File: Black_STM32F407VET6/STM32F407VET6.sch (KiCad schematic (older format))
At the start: 97 parts, among them J1 T0, J10 - HotBed +, J11 Heater0, J12 X-, J13 Y-, J14 Z-, J15 Z+, J16 USB_B, J17 X_logic, J18 Y_logic, J19 Z_logic, J2 T1, J20 E0_logic, J22 Left, J23 EXP2, J24 LCD2004, J25 Bottom, J26 Right, J27 Z_motor, J28 LIGHTS, J29 Z, J3 TB, J30 Z, J33 X_motor, J34 Y_motor, J36 E0_motor, J38 X, J39 Y, J4 TC, J41 E0, J43 Heater1, J44 COM, J47 I2C, J48 SPI, J49 SPI, J5 + VIN -, J50 SDIO, J51 Servo, J52 Servo, J53 PowerSelect, J54 Power, J55 PD11, J56 Power, J6 Fan3, J7 Fan2, J8 Fan1, J9 Fan0, Q1 BCX70, Q10 BCX70, Q11 BCX70, Q12 IRLR8726PBF, Q13 IRLR8726PBF, Q14 IRLR8726PBF, Q2 BCX70, Q3 BCX70, Q4 IRLML0030TRPBF, Q5 BCX70, Q6 IRLML0030TRPBF, Q7 IRLML0030TRPBF, Q8 IRLML0030TRPBF, Q9 BCX70, SW1 Boot0, U5 AT24CS01-SSHM

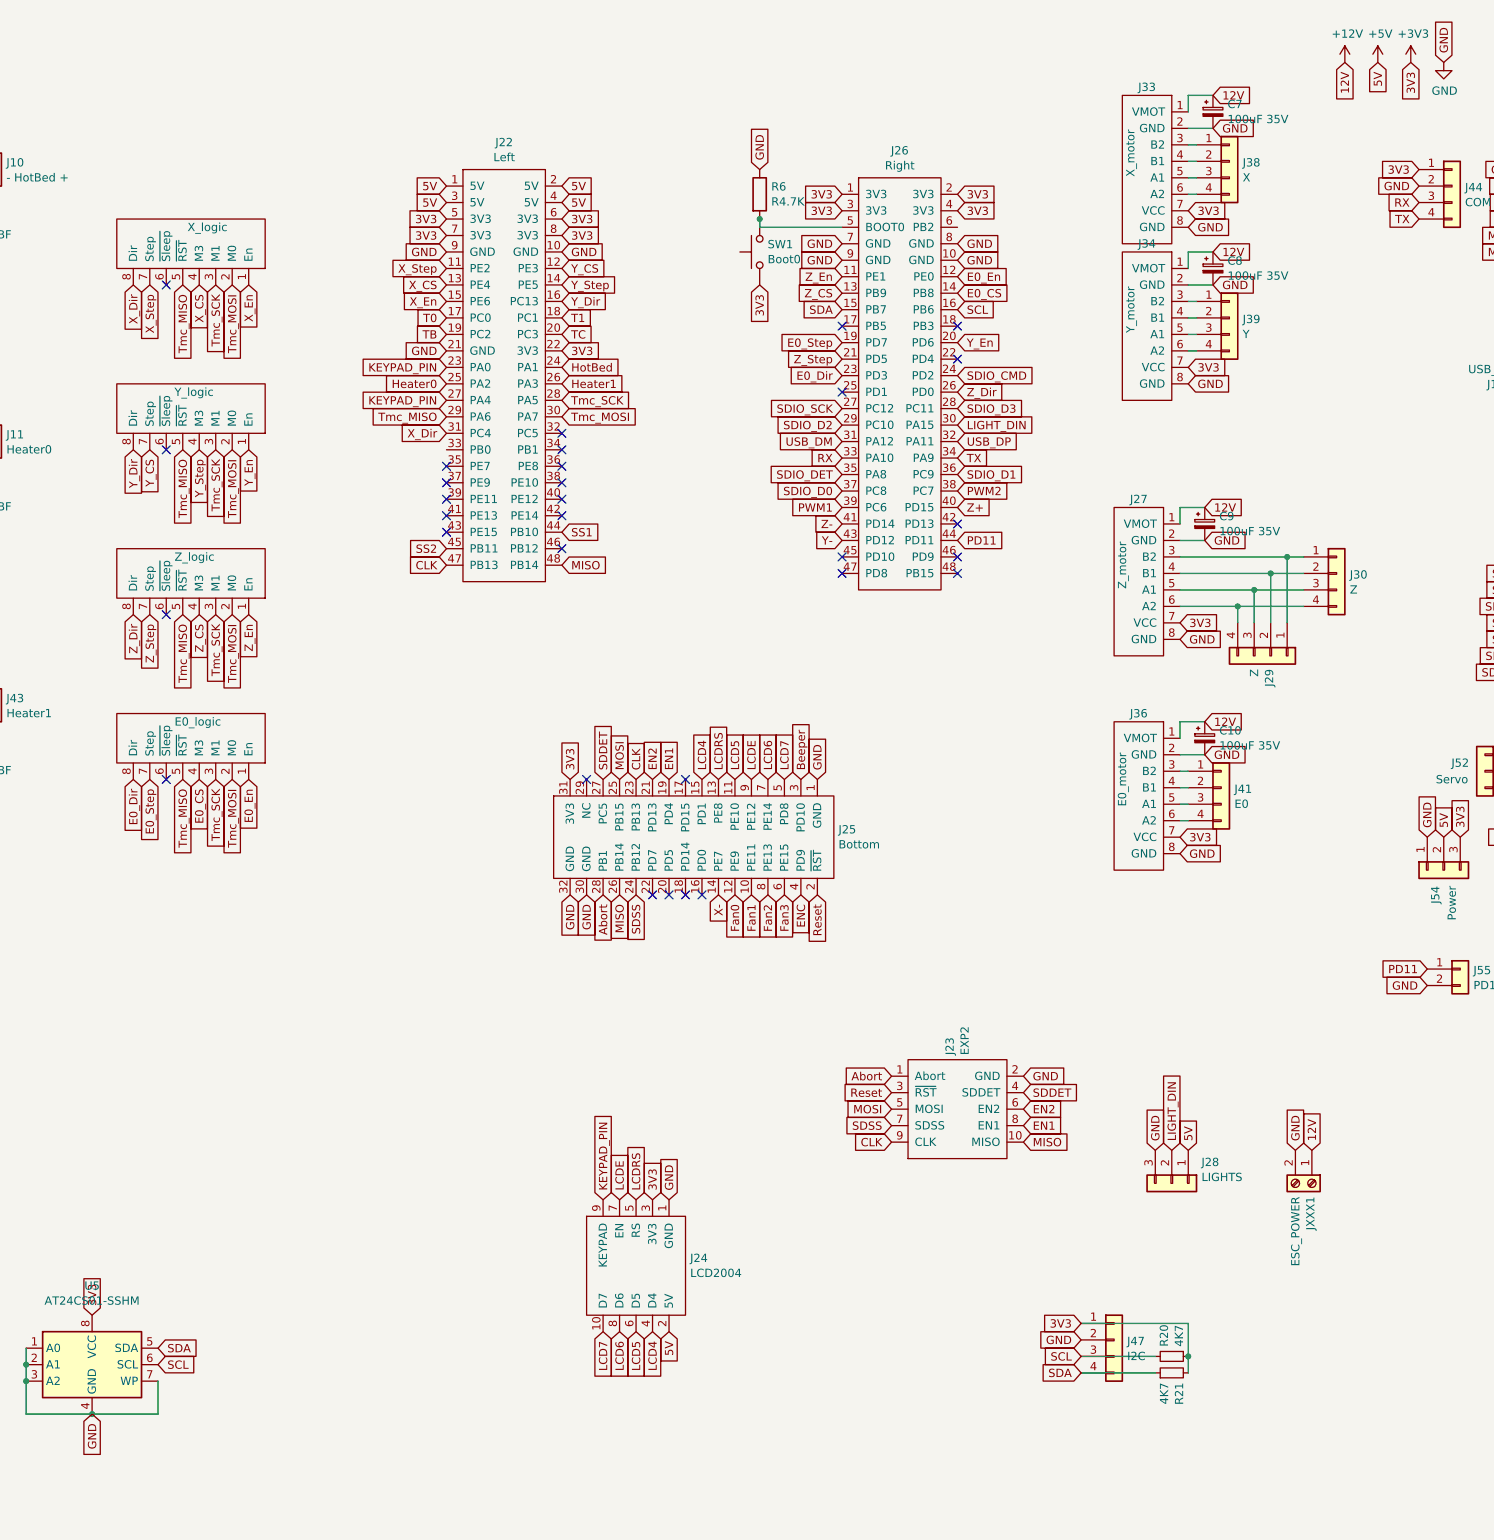
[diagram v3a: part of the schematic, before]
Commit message: Rework of the PCB, made footprint for the motor drivers.
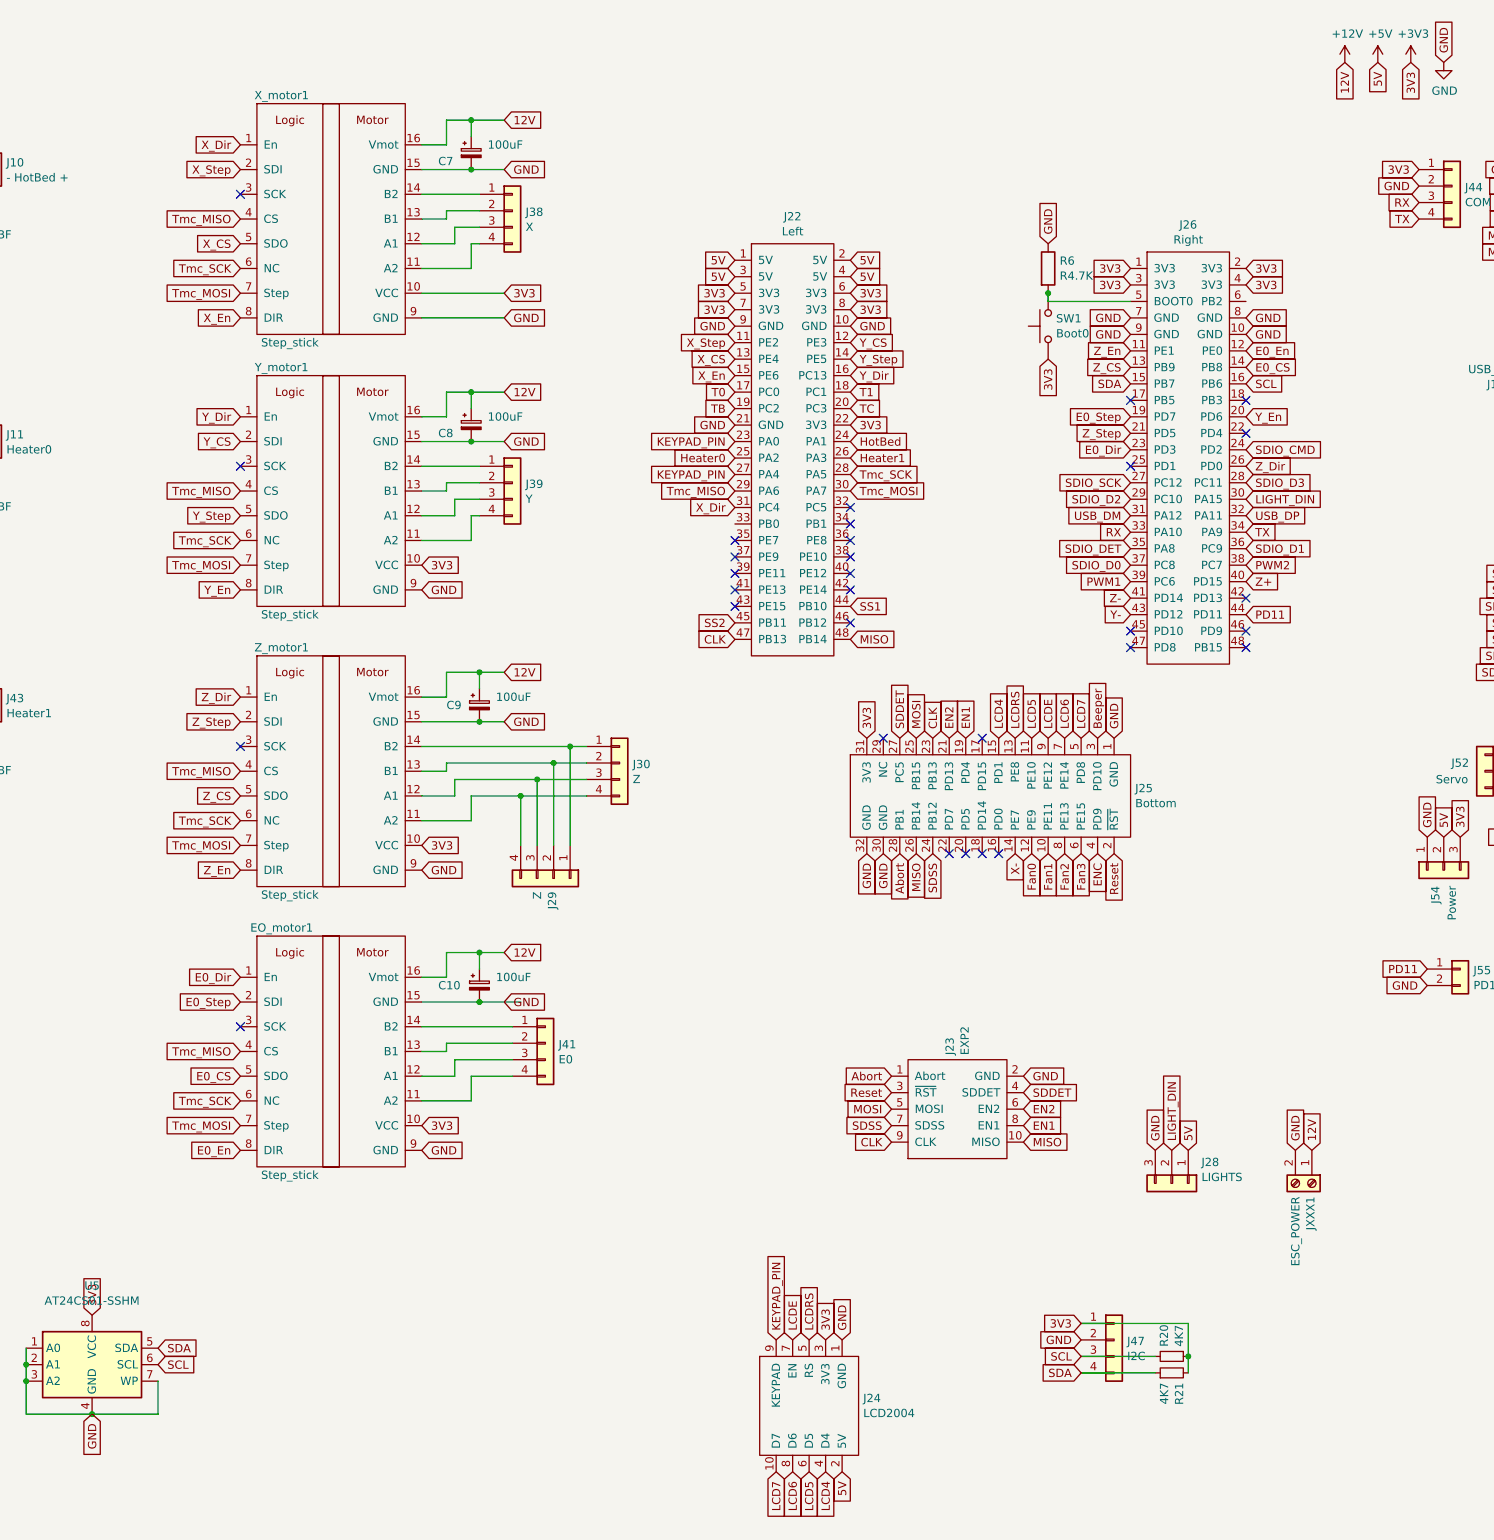
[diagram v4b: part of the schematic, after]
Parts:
- removed J17: X_logic, Connector_PinSocket_2.54mm:PinSocket_1x08_P2.54mm_Vertical, symbol STM32F407VET6-rescue:DRV_logic-STM32F407VET6
- removed J18: Y_logic, Connector_PinSocket_2.54mm:PinSocket_1x08_P2.54mm_Vertical, symbol STM32F407VET6-rescue:DRV_logic-STM32F407VET6
- removed J19: Z_logic, Connector_PinSocket_2.54mm:PinSocket_1x08_P2.54mm_Vertical, symbol STM32F407VET6-rescue:DRV_logic-STM32F407VET6
- removed J20: E0_logic, Connector_PinSocket_2.54mm:PinSocket_1x08_P2.54mm_Vertical, symbol STM32F407VET6-rescue:DRV_logic-STM32F407VET6
- removed J27: Z_motor, Connector_PinSocket_2.54mm:PinSocket_1x08_P2.54mm_Vertical, symbol STM32F407VET6:DRV_motor
- removed J33: X_motor, Connector_PinSocket_2.54mm:PinSocket_1x08_P2.54mm_Vertical, symbol STM32F407VET6:DRV_motor
- removed J34: Y_motor, Connector_PinSocket_2.54mm:PinSocket_1x08_P2.54mm_Vertical, symbol STM32F407VET6:DRV_motor
- removed J36: E0_motor, Connector_PinSocket_2.54mm:PinSocket_1x08_P2.54mm_Vertical, symbol STM32F407VET6:DRV_motor
- added EO_motor1, X_motor1, Y_motor1, Z_motor1: Step_stick, Motor_driver:Motor, symbol Motor_driver:Step_stick
- C10, C7, C8, C9: value 100uF 35V -> 100uF
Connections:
- net +12V: now also EO_motor1.16 (Vmot), X_motor1.16 (Vmot), Y_motor1.16 (Vmot), Z_motor1.16 (Vmot)
- net +3V3: now also EO_motor1.10 (VCC), X_motor1.10 (VCC), Y_motor1.10 (VCC), Z_motor1.10 (VCC)
- net E0_CS: now also EO_motor1.5 (SDO)
- net E0_Dir: now also EO_motor1.1 (En)
- net E0_En: now also EO_motor1.8 (DIR)
- net E0_Step: now also EO_motor1.2 (SDI)
- net GND: now also EO_motor1.15 (GND), EO_motor1.9 (GND), X_motor1.15 (GND), X_motor1.9 (GND), Y_motor1.15 (GND), Y_motor1.9 (GND), Z_motor1.15 (GND), Z_motor1.9 (GND)
- net Tmc_MISO: now also EO_motor1.4 (CS), X_motor1.4 (CS), Y_motor1.4 (CS), Z_motor1.4 (CS)
- net Tmc_MOSI: now also EO_motor1.7 (Step), X_motor1.7 (Step), Y_motor1.7 (Step), Z_motor1.7 (Step)
- net Tmc_SCK: now also EO_motor1.6 (NC), X_motor1.6 (NC), Y_motor1.6 (NC), Z_motor1.6 (NC)
- net X_CS: now also X_motor1.5 (SDO)
- net X_Dir: now also X_motor1.1 (En)
- net X_En: now also X_motor1.8 (DIR)
- net X_Step: now also X_motor1.2 (SDI)
- net Y_CS: now also Y_motor1.2 (SDI)
- net Y_Dir: now also Y_motor1.1 (En)
- net Y_En: now also Y_motor1.8 (DIR)
- net Y_Step: now also Y_motor1.5 (SDO)
- net Z_CS: now also Z_motor1.5 (SDO)
- net Z_Dir: now also Z_motor1.1 (En)
- net Z_En: now also Z_motor1.8 (DIR)
- net Z_Step: now also Z_motor1.2 (SDI)
- net at J38.1 (Pin_1): now also X_motor1.14 (B2)
- net at J38.2 (Pin_2): now also X_motor1.13 (B1)
- net at J38.3 (Pin_3): now also X_motor1.12 (A1)
- net at J38.4 (Pin_4): now also X_motor1.11 (A2)
- net at J39.1 (Pin_1): now also Y_motor1.14 (B2)
- net at J39.2 (Pin_2): now also Y_motor1.13 (B1)
- net at J39.3 (Pin_3): now also Y_motor1.12 (A1)
- net at J39.4 (Pin_4): now also Y_motor1.11 (A2)
- net at J41.1 (Pin_1): now also EO_motor1.14 (B2)
- net at J41.2 (Pin_2): now also EO_motor1.13 (B1)
- net at J41.3 (Pin_3): now also EO_motor1.12 (A1)
- net at J41.4 (Pin_4): now also EO_motor1.11 (A2)
- net at J29.1 (Pin_1), J30.1 (Pin_1): now also Z_motor1.14 (B2)
- net at J29.2 (Pin_2), J30.2 (Pin_2): now also Z_motor1.13 (B1)
- net at J29.3 (Pin_3), J30.3 (Pin_3): now also Z_motor1.12 (A1)
- net at J29.4 (Pin_4), J30.4 (Pin_4): now also Z_motor1.11 (A2)
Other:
- moved on the sheet: C10, C7, C8, C9, J22, J24, J25, J26, J29, J30, J38, J39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
